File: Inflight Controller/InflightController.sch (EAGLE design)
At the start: 8 parts

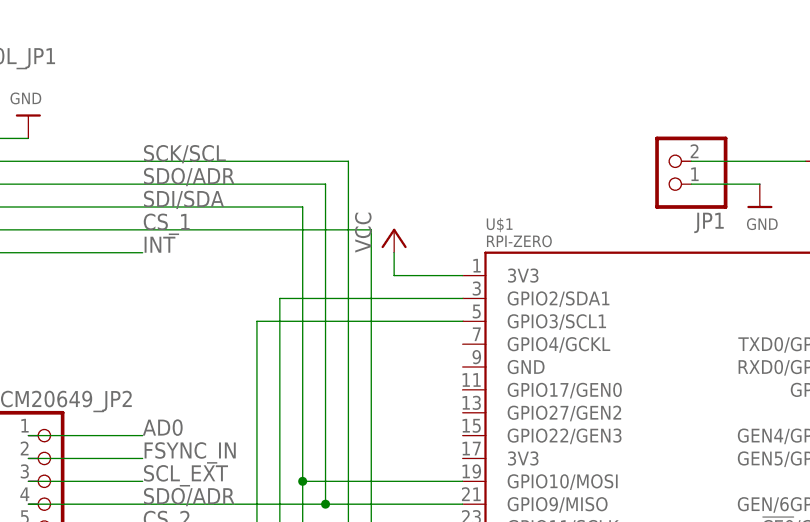
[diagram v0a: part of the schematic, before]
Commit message: Fixed VCC routing from PI
5/24/21
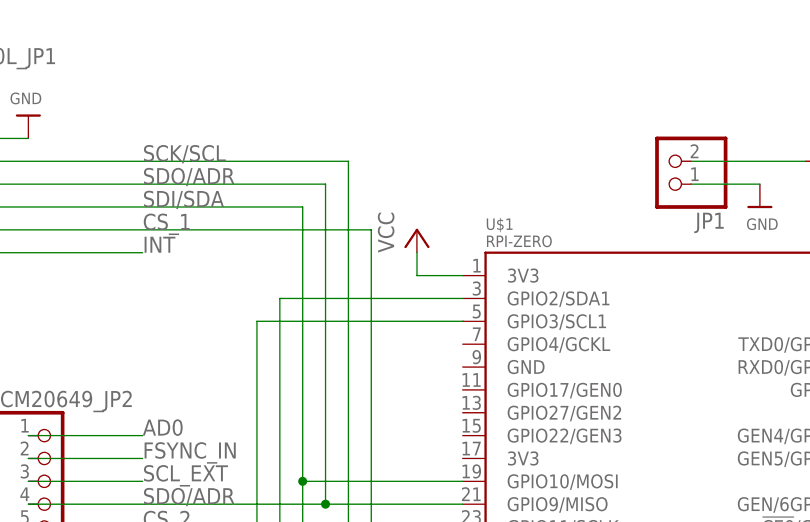
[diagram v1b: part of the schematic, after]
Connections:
- removed net 3V3@1: U$1.3V3@1
- net VCC: now also U$1.3V3@1
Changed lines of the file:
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@@
 <part name="BMP390L_JP1" library="microbuilder" deviceset="HEADER-1X8" device="70MIL"/>
 <part name="P+5" library="supply1" library_urn="urn:adsk.eagle:library:371" deviceset="VCC" device=""/>
-<part name="P+2" library="supply1" library_urn="urn:adsk.eagle:library:371" deviceset="VCC" device=""/>
 <part name="JP1" library="pinhead" library_urn="urn:adsk.eagle:library:325" deviceset="PINHD-1X2" device="" package3d_urn="urn:adsk.eagle:package:22435/2"/>
 <part name="U$3" library="microbuilder" deviceset="GND" device=""/>
@@
 <part name="GND2" library="supply1" library_urn="urn:adsk.eagle:library:371" deviceset="GND" device=""/>
 <part name="R2" library="resistor-shunt" library_urn="urn:adsk.eagle:library:346" deviceset="SMK" device="" package3d_urn="urn:adsk.eagle:package:25215/1"/>
+<part name="P+2" library="supply1" library_urn="urn:adsk.eagle:library:371" deviceset="VCC" device=""/>
 </parts>
 <sheets>
@@
 <attribute name="VALUE" x="25.4" y="119.38" size="1.778" layer="96" rot="R90"/>
 </instance>
-<instance part="P+2" gate="VCC" x="83.82" y="101.6" smashed="yes">
-<attribute name="VALUE" x="81.28" y="99.06" size="1.778" layer="96" rot="R90"/>
-</instance>
 <instance part="JP1" gate="G$1" x="114.3" y="109.22" smashed="yes" rot="R180">
 <attribute name="NAME" x="120.65" y="103.505" size="1.778" layer="95" rot="R180"/>
@@
 <attribute name="NAME" x="135.9916" y="107.95" size="1.778" layer="95" rot="R180"/>
 <attribute name="VALUE" x="138.43" y="112.141" size="1.778" layer="96" rot="R180"/>
+</instance>
+<instance part="P+2" gate="VCC" x="86.36" y="101.6" smashed="yes">
+<attribute name="VALUE" x="83.82" y="99.06" size="1.778" layer="96" rot="R90"/>
 </instance>
 </instances>
@@
 <pinref part="BMP390L_JP1" gate="A" pin="1"/>
 <pinref part="P+5" gate="VCC" pin="VCC"/>
+</segment>
+<segment>
+<pinref part="P+2" gate="VCC" pin="VCC"/>
+<wire x1="86.36" y1="99.06" x2="86.36" y2="96.52" width="0.1524" layer="91"/>
+<pinref part="U$1" gate="G$1" pin="3V3@1"/>
+<wire x1="86.36" y1="96.52" x2="91.44" y2="96.52" width="0.1524" layer="91"/>
 </segment>
 </net>
@@
 </segment>
 </net>
-<net name="3V3@1" class="2">
-<segment>
-<wire x1="91.44" y1="96.52" x2="83.82" y2="96.52" width="0.1524" layer="91"/>
-<wire x1="83.82" y1="96.52" x2="83.82" y2="99.06" width="0.1524" layer="91"/>
-<pinref part="P+2" gate="VCC" pin="VCC"/>
-<pinref part="U$1" gate="G$1" pin="3V3@1"/>
-</segment>
-</net>

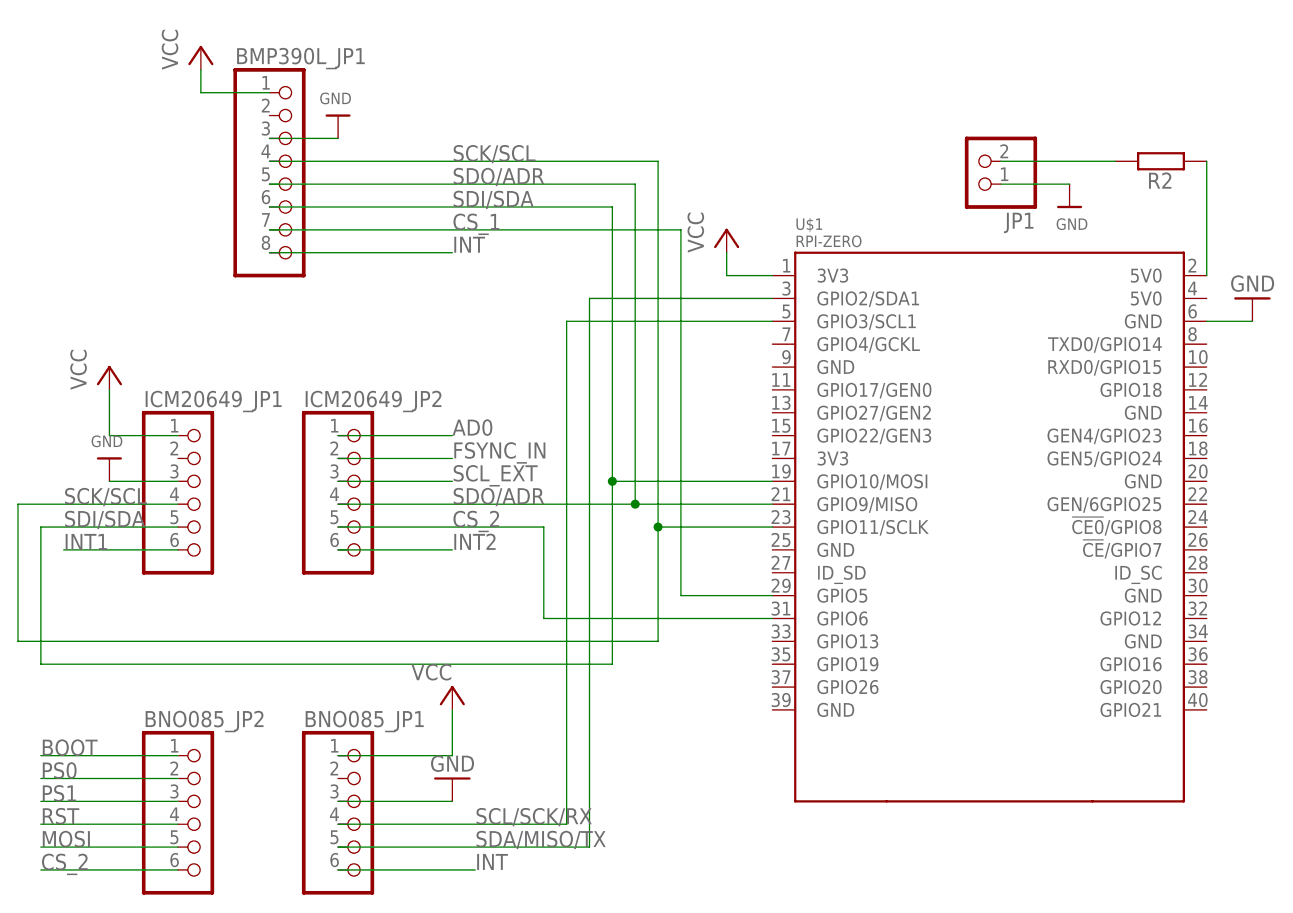
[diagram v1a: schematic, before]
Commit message: Fixed more traces
5/24/21
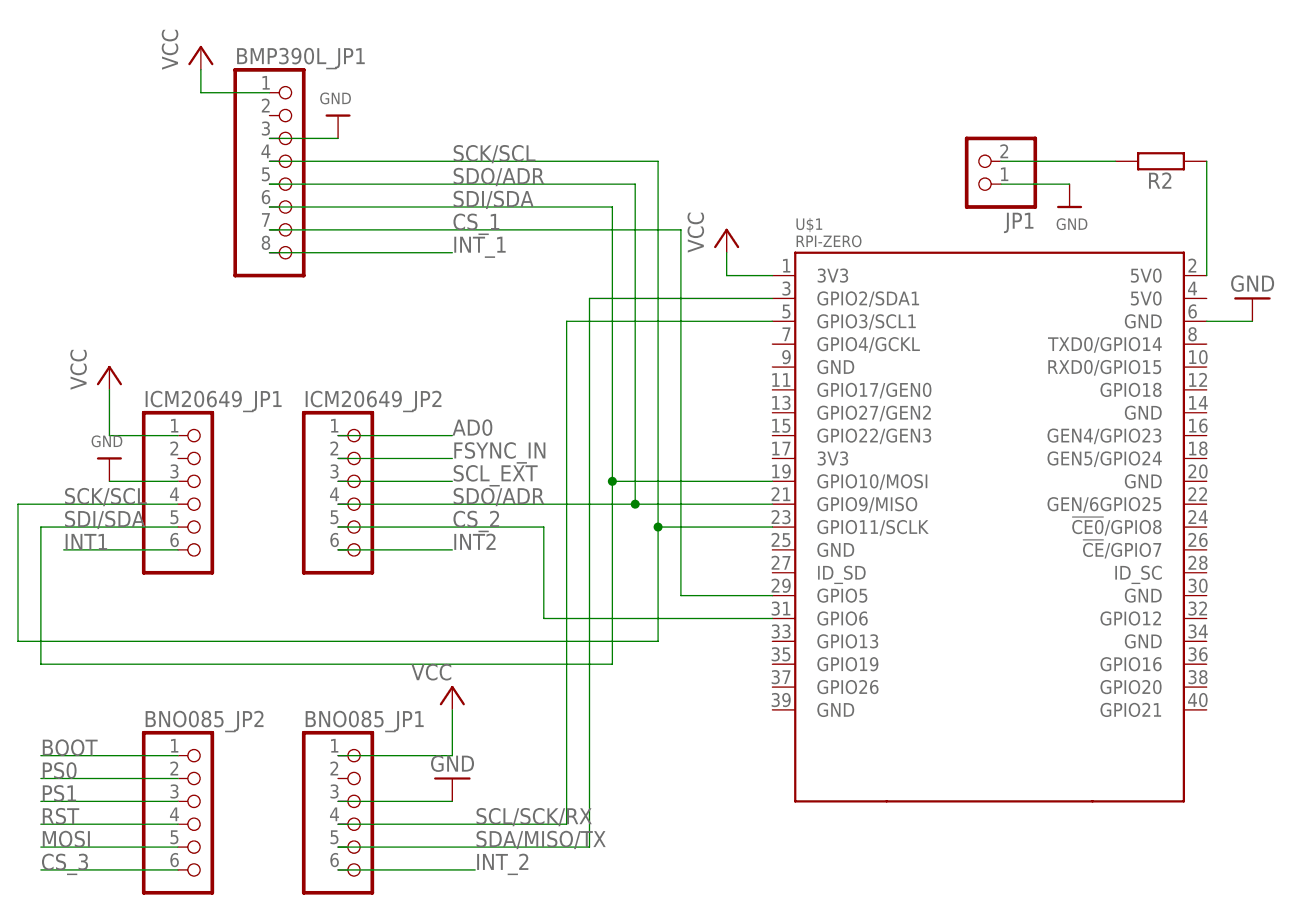
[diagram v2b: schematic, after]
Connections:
- removed net INT: BMP390L_JP1.8, BNO085_JP1.6
- new net CS_3: BNO085_JP2.6
- new net INT_1: BMP390L_JP1.8
- new net INT_2: BNO085_JP1.6
- net CS_2: no longer BNO085_JP2.6
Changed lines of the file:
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@@
 </segment>
 </net>
-<net name="INT" class="0">
+<net name="INT_2" class="0">
 <segment>
 <pinref part="BNO085_JP1" gate="A" pin="6"/>
 <wire x1="43.18" y1="30.48" x2="58.42" y2="30.48" width="0.1524" layer="91"/>
 <label x="58.42" y="30.48" size="1.778" layer="95"/>
-</segment>
-<segment>
-<pinref part="BMP390L_JP1" gate="A" pin="8"/>
-<wire x1="35.56" y1="99.06" x2="55.88" y2="99.06" width="0.1524" layer="91"/>
-<label x="55.88" y="99.06" size="1.778" layer="95"/>
 </segment>
 </net>
@@
 </net>
 <net name="CS_2" class="0">
-<segment>
-<pinref part="BNO085_JP2" gate="A" pin="6"/>
-<wire x1="25.4" y1="30.48" x2="10.16" y2="30.48" width="0.1524" layer="91"/>
-<label x="10.16" y="30.48" size="1.778" layer="95"/>
-</segment>
 <segment>
 <wire x1="43.18" y1="68.58" x2="66.04" y2="68.58" width="0.1524" layer="91"/>
@@
 </segment>
 </net>
+<net name="INT_1" class="0">
+<segment>
+<pinref part="BMP390L_JP1" gate="A" pin="8"/>
+<wire x1="35.56" y1="99.06" x2="55.88" y2="99.06" width="0.1524" layer="91"/>
+<label x="55.88" y="99.06" size="1.778" layer="95"/>
+</segment>
+</net>
+<net name="CS_3" class="0">
+<segment>
+<pinref part="BNO085_JP2" gate="A" pin="6"/>
+<wire x1="25.4" y1="30.48" x2="10.16" y2="30.48" width="0.1524" layer="91"/>
+<label x="10.16" y="30.48" size="1.778" layer="95"/>
+</segment>
+</net>
